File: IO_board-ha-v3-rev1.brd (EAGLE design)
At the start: 99 x 102 mm, 35 parts, among them J1 4-PIN-CON-1759017, J2 4-PIN-CON-1759017

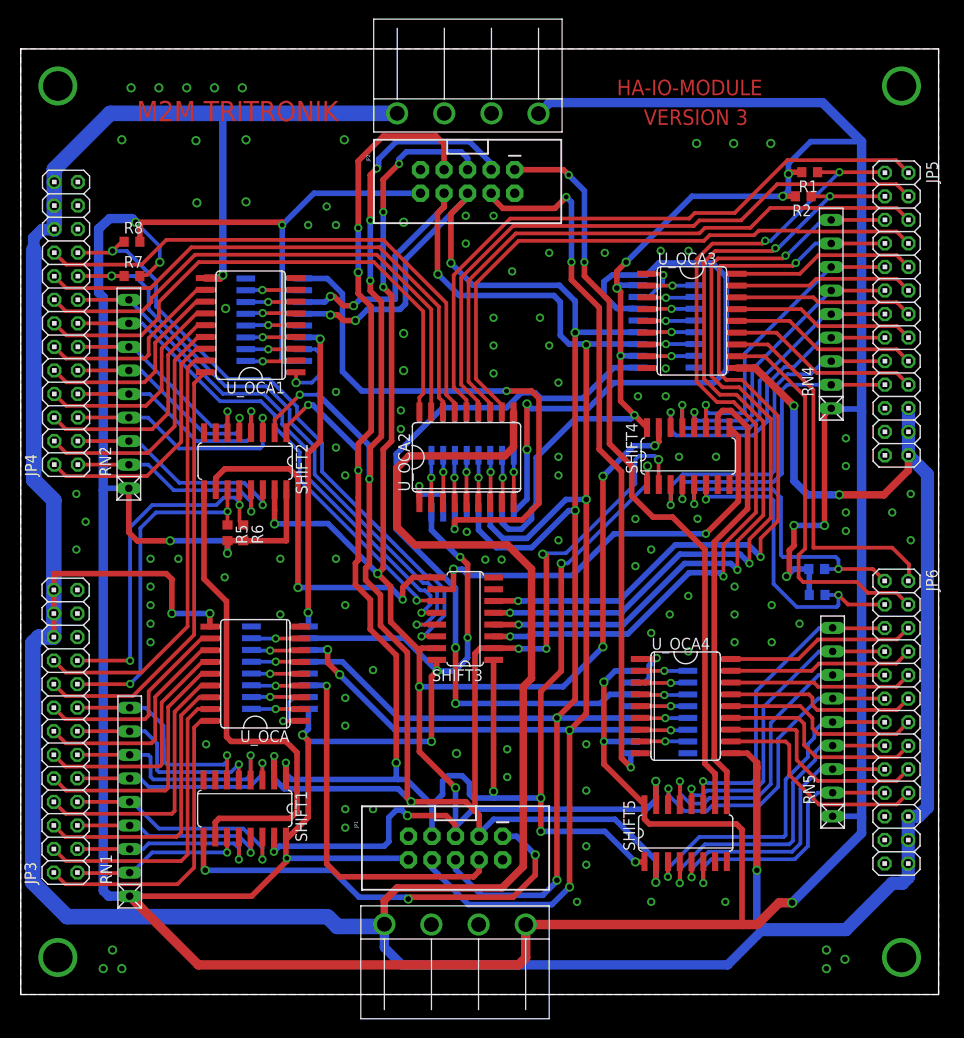
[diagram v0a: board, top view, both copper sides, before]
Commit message: Uptade all fixed design
This is whole new update for all device version
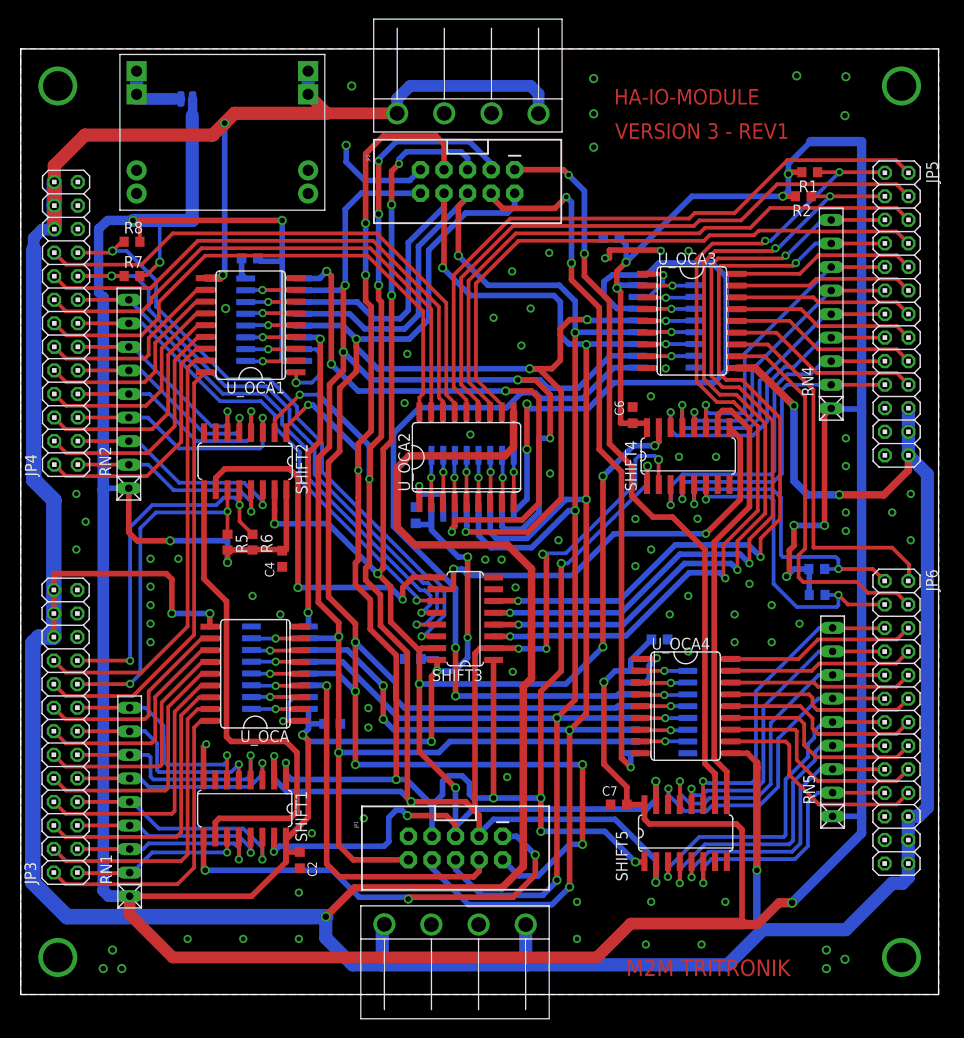
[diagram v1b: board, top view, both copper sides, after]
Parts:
- added C10, C11, C12, C2, C4, C5, C6, C7, C8, C9: 100nF, rcl:C0603K
- added U$1: DCDCMODULE_SMALL, bontor:DCDCMODULE-SMALL
- added U$2: DOUBLE_SMALL_PAD, maul:DOUBLE_SMALL_PAD
- moved R6 1.41 mm to (25.0, 48.8)
- moved R5 1.00 mm to (22.3, 48.8)
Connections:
- new net MR: JP1.10, JP2.10, SHIFTOUTA.10, SHIFTOUTB.10, SHIFTOUTC.10, SHIFTOUTD.10, SHIFTOUTE.10
- new net N$12: U$1.OUTP#1, U$1.OUTP#2, U$2.PAD1
- new net OE: JP1.2, JP2.2, SHIFTOUTA.13, SHIFTOUTB.13, SHIFTOUTC.13, SHIFTOUTD.13, SHIFTOUTE.13
- net +12V: now also J1.1, J2.4, U$1.INP#1, U$1.INP#2
- net GND: now also C10.1, C11.1, C12.1, C2.1, C4.1, C5.1, C6.1, C7.1, C8.1, C9.1, U$1.INM#1, U$1.INM#2, U$1.OUTM#1, U$1.OUTM#2; no longer JP1.2, JP2.2, SHIFTOUTA.13, SHIFTOUTB.13, SHIFTOUTC.13, SHIFTOUTD.13, SHIFTOUTE.13
- net VCC: now also C10.2, C11.2, C12.2, C2.2, C4.2, C5.2, C6.2, C7.2, C8.2, C9.2, U$2.PAD2; no longer J1.1, J2.4, JP1.10, JP2.10, SHIFTOUTA.10, SHIFTOUTB.10, SHIFTOUTC.10, SHIFTOUTD.10, SHIFTOUTE.10
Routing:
- net OE: track 0.00 -> 235.2 mm, vias 0 -> 9
- net MR: track 0.00 -> 187.1 mm, vias 0 -> 6
- net VCC: track 648.2 -> 575.5 mm, vias 23 -> 19
- net +12V: track 470.7 -> 513.5 mm, vias 6 -> 8
- net GND: track 6.62 -> 29.6 mm, vias 110 -> 84
- net N$12: track 0.00 -> 7.77 mm
- net SHCP: track 191.5 -> 194.1 mm, vias 9 -> 7
- net N$37: track 59.7 -> 61.9 mm, vias 2 -> 4
- net 2-2: track 37.7 -> 39.1 mm
- net STCP: track 186.2 -> 187.2 mm, vias 7 -> 5
- net PL: track 210.4 -> 209.4 mm
- net 2-1: track 36.9 -> 37.9 mm
- net CE: track 209.4 -> 208.5 mm
- net CLK: track 220.4 -> 219.7 mm
- net 3-5: track 93.8 -> 94.6 mm
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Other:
- board text added: "VERSION 3 - REV1"
- board text removed: "VERSION 3"

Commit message: Upgrade to version 5
With LAN Ethernet ENC28J60; adding relay for restarting 12V modules
(Driver & IO).
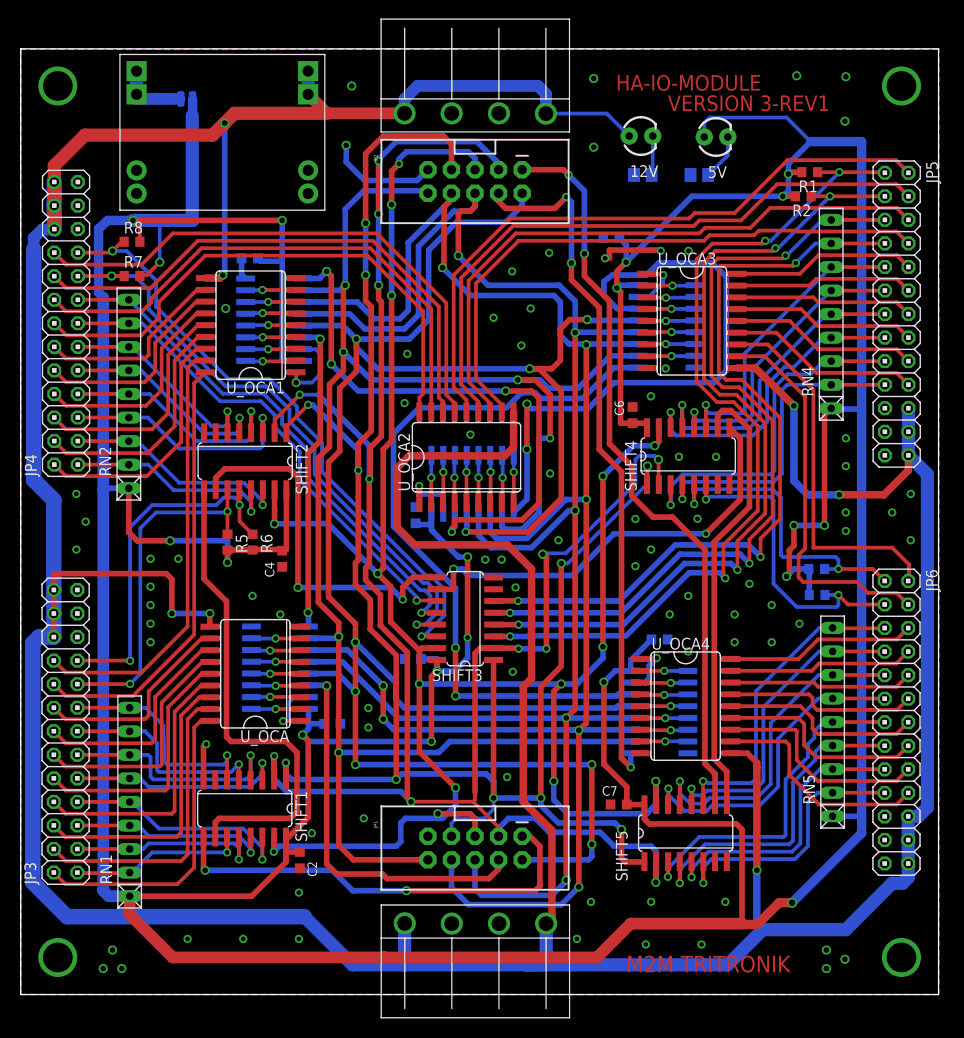
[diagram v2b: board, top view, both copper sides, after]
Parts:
- added 12V, 5V: (no value), SparkFun-LED:LED3MM
- added R10: 220, rcl:R0805
- added R9: 1k, rcl:R0805
- moved J2 2.20 mm to (49.0, 3.55)
- moved JP1 2.10 mm to (49.0, 15.8)
- moved J1 0.80 mm to (49.0, 99.2)
- moved JP2 0.80 mm to (49.0, 87.7)
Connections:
- new net N$13: 12V.K, R9.1
- new net N$17: 5V.K, R10.1
- net +12V: now also 12V.A
- net GND: now also R10.2, R9.2
- net VCC: now also 5V.A
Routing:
- net VCC: track 575.5 -> 589.8 mm
- net N$17: track 0.00 -> 4.98 mm
- net CE: track 208.5 -> 213.4 mm, vias 13 -> 15
- net +12V: track 513.5 -> 509.0 mm, vias 8 -> 7
- net N$13: track 0.00 -> 4.25 mm
- net MR: track 187.1 -> 190.3 mm
- net PL: track 209.4 -> 212.2 mm, vias 12 -> 11
- net SR_DS: track 39.7 -> 41.8 mm
- net STCP: track 187.2 -> 189.3 mm
- net SHCP: track 194.1 -> 195.0 mm
- net GND: track 29.6 -> 30.4 mm, vias 84 -> 83
- net Q7_2: track 81.7 -> 80.9 mm
- net Q7: track 48.1 -> 47.5 mm, vias 3 -> 2
- net SR_DS_2: track 75.4 -> 74.9 mm
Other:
- board text added: "VERSION 3-REV1"
- board text removed: "VERSION 3 - REV1"
